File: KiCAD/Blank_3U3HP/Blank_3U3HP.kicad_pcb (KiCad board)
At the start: 2 copper layers, 15 x 128.5 mm, 2 parts

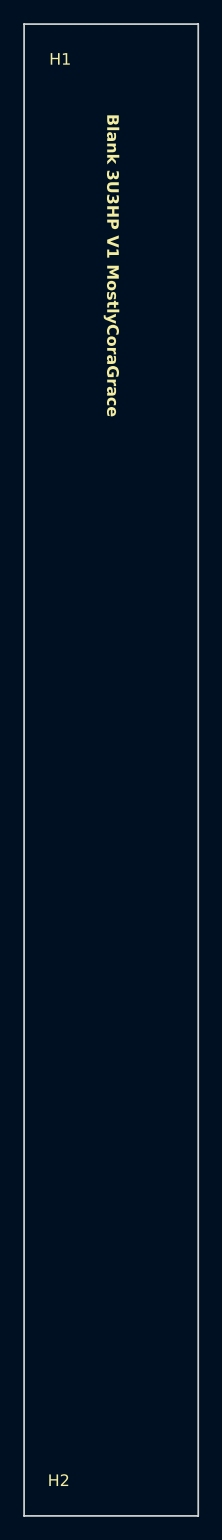
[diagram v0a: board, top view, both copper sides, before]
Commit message: removed all front silkscreen, and flipped most modules, to make the boards 'cleaner'.
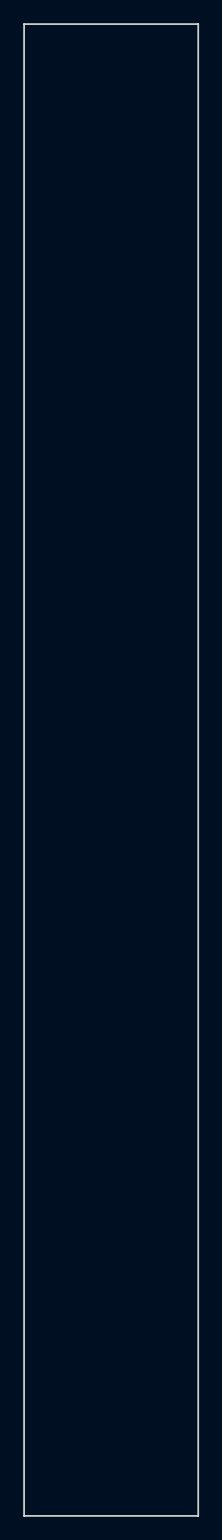
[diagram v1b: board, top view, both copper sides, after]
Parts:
- H1, H2: moved to B.Cu
- turned H1 to 180 degrees
- turned H2 to 180 degrees

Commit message: added copper fills to every module, to maybe possibly increase structural rigidity.
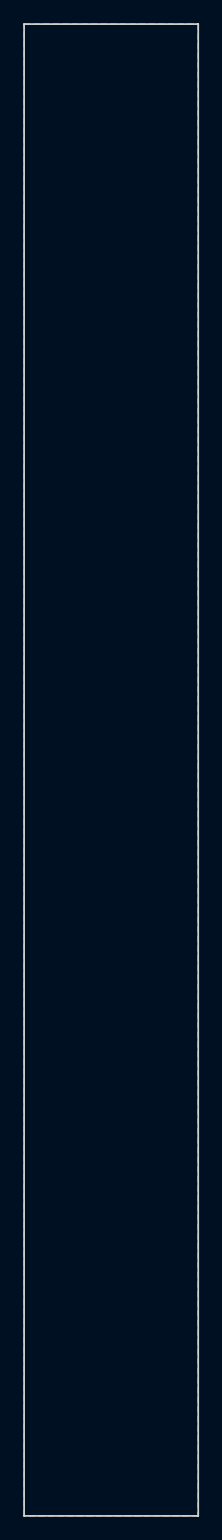
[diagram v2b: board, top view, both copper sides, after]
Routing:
- added copper zone on B.Cu, net (none)
- added copper zone on F.Cu, net (none)
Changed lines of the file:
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@@
+		)
+	)
+	(zone
+		(net 0)
+		(net_name "")
+		(layers "F&B.Cu")
+		(hatch edge 0.5)
+		(connect_pads
+			(clearance 0.5)
+		)
+		(min_thickness 0.25)
+		(filled_areas_thickness no)
+		(fill yes
+			(thermal_gap 0.5)
+			(thermal_bridge_width 0.5)
+			(island_removal_mode 1)
+			(island_area_min 10)
+		)
+		(polygon
+			(pts
+				(xy 0 2.413) (xy 14.986 2.413) (xy 14.986 130.937) (xy 0 130.937)
+			)
 		)
 	)
